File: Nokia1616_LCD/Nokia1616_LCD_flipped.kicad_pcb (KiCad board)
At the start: 2 copper layers, 35.1 x 55.8 mm, 5 parts, among them P1 CONN_01X08, Q1 BC547_BEC_123

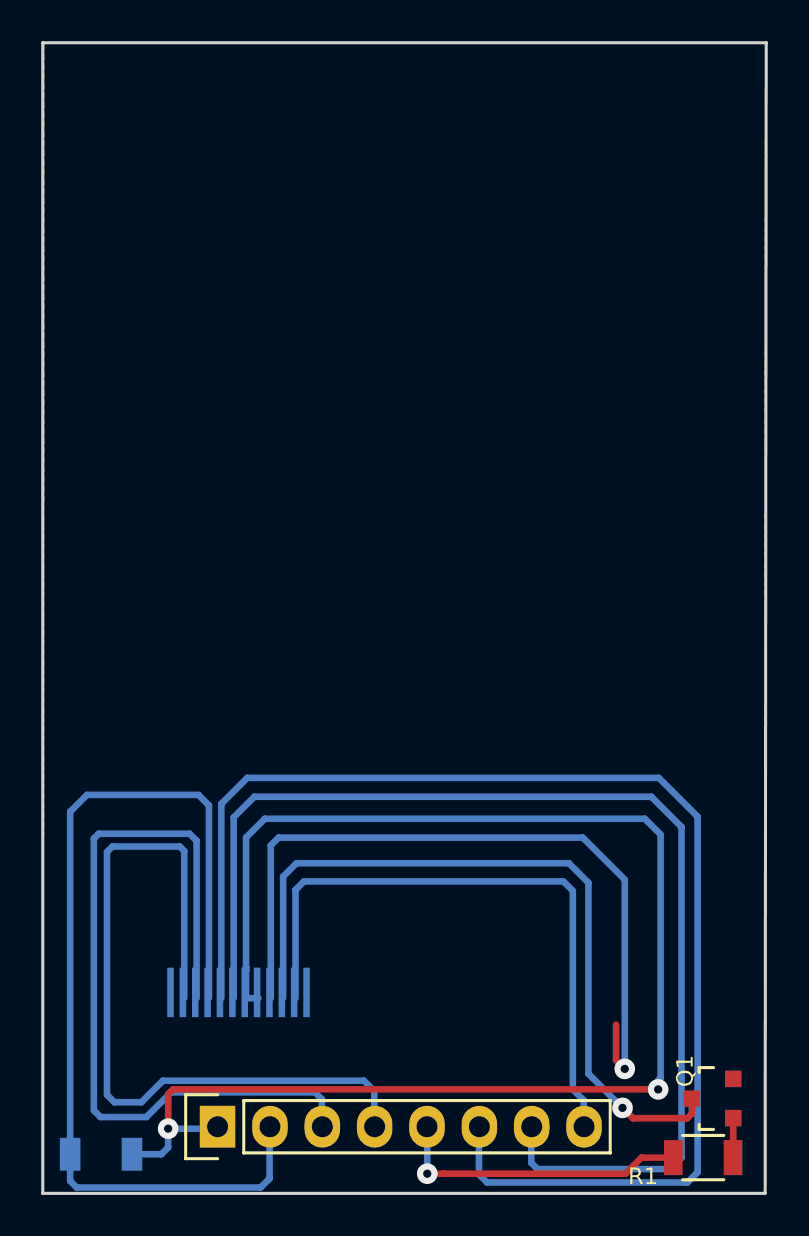
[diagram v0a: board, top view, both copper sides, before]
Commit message: Too many untracked changes: LCD boards update and switch to KiCAD version 5
Update the Nokia LCD breakout boards
Add more KiCAD simulation projects
Update most projects to KiCAD version 5
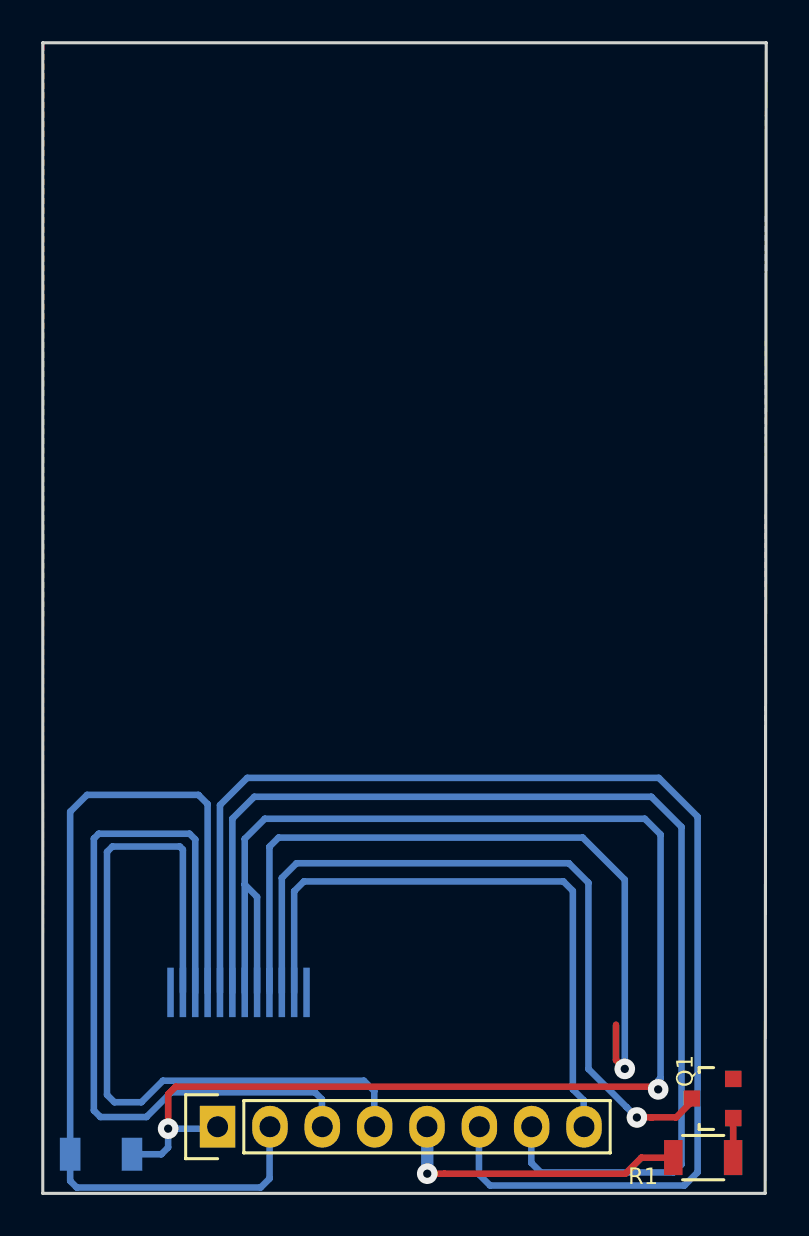
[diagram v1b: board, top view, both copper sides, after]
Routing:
- net VCC: track 72.5 -> 77.1 mm
- net LED: track 14.5 -> 16.7 mm
- net LED-: track 37.4 -> 36.6 mm
- net GND: track 84.1 -> 83.5 mm
